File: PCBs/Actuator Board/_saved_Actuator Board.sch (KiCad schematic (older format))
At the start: 14 parts

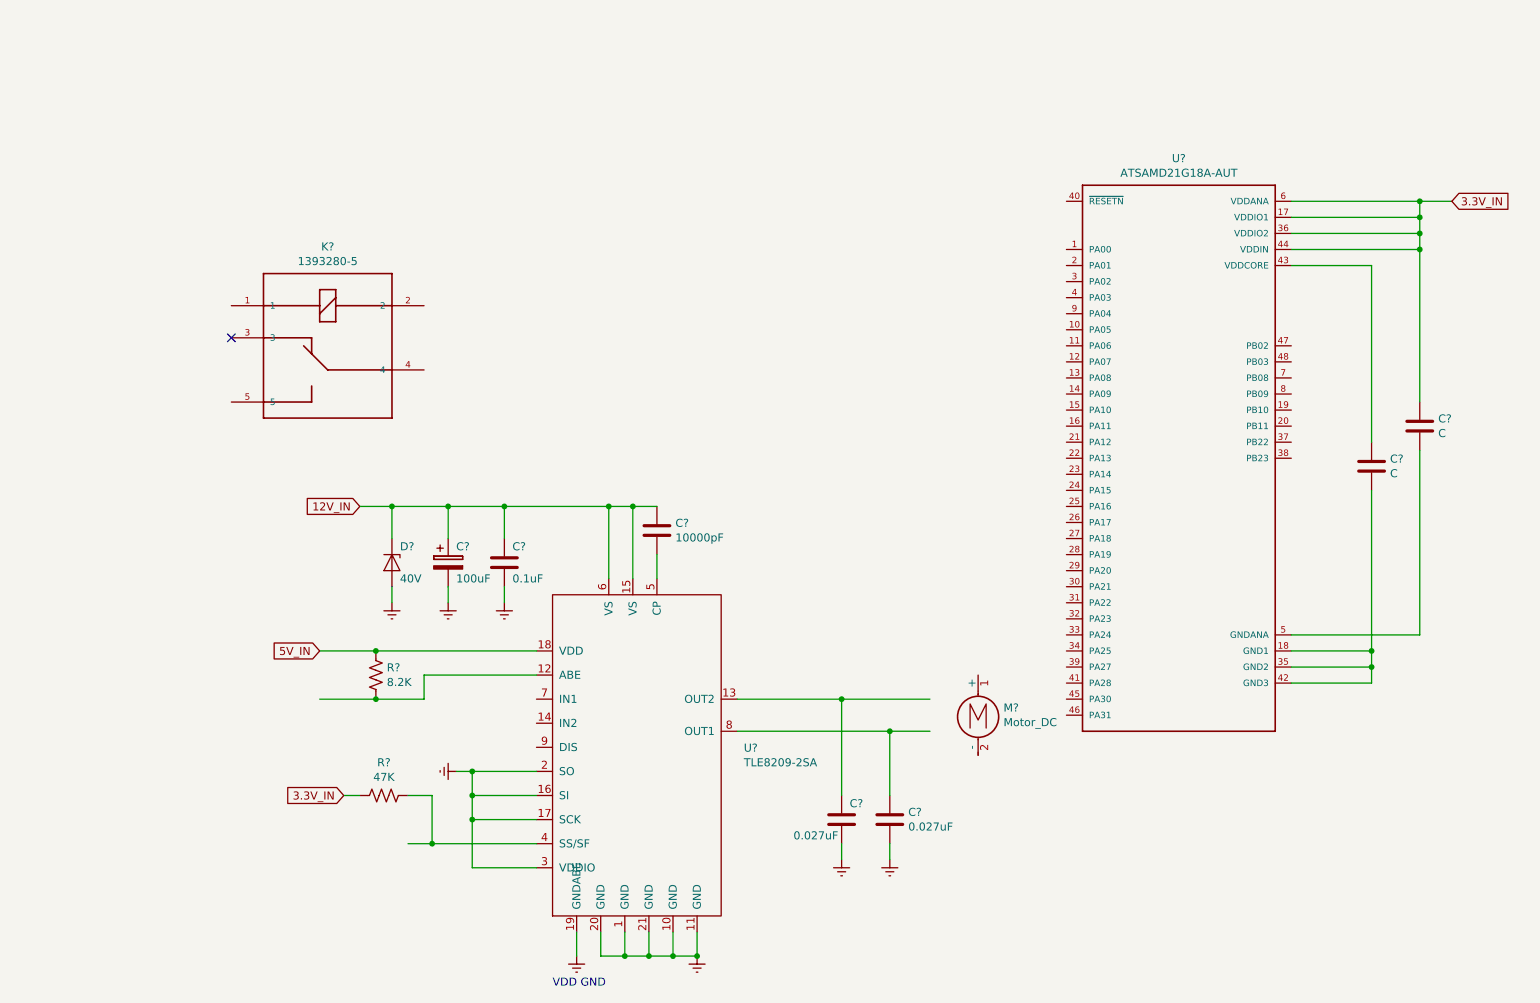
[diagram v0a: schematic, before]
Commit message: Started Relay
finish relay values
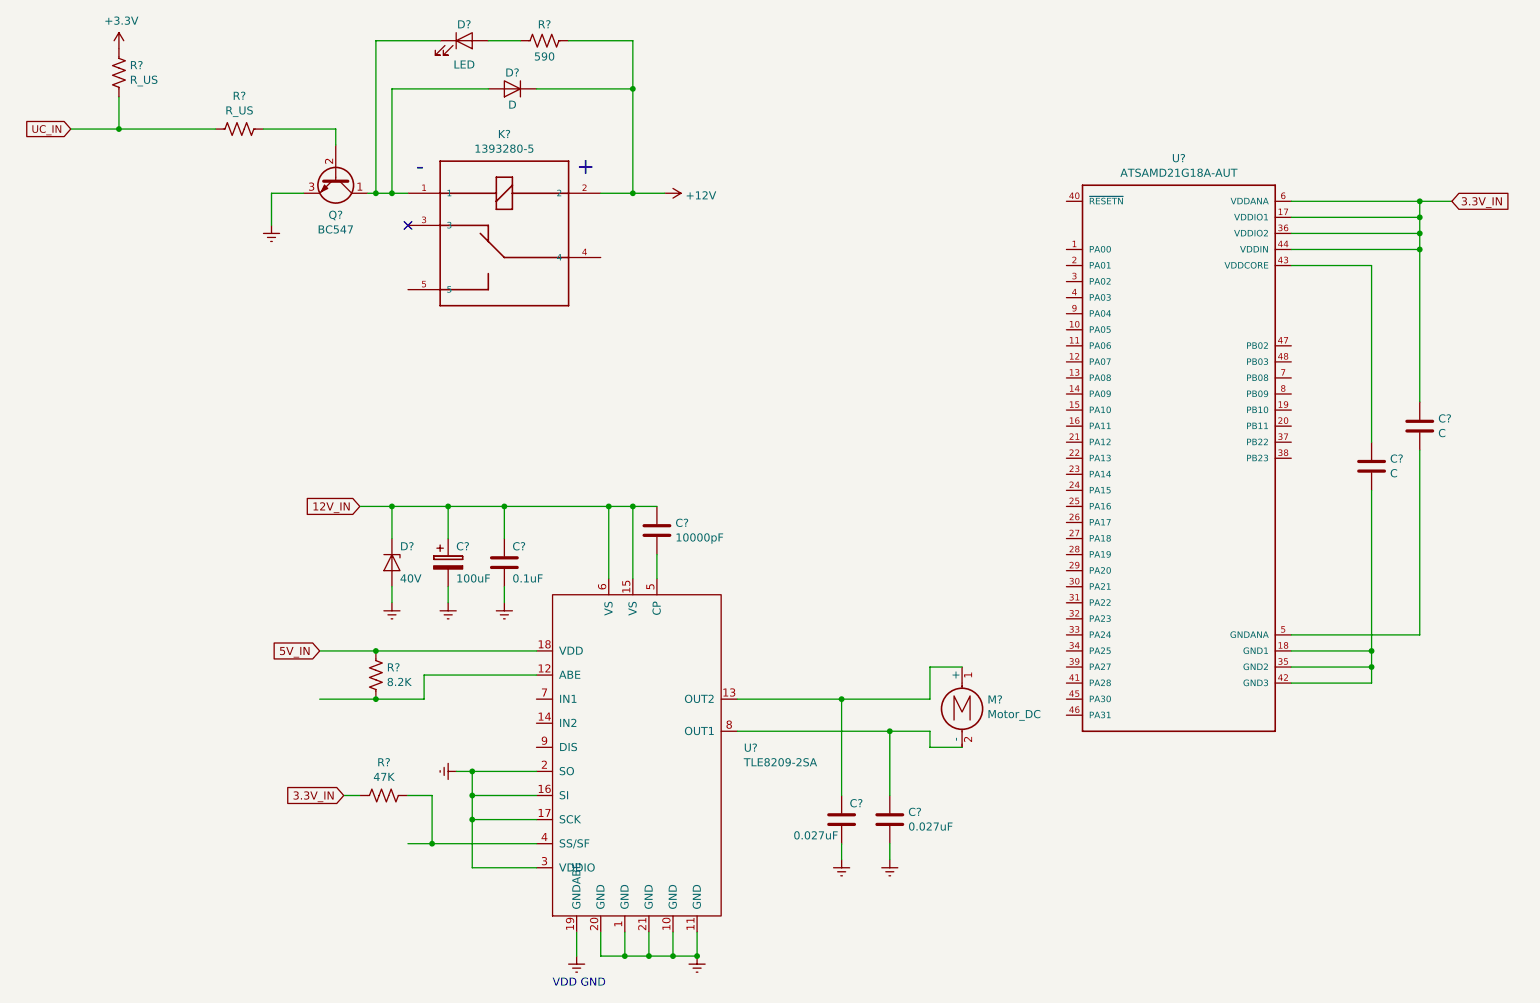
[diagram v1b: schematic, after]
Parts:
- added D?: LED, symbol Device:LED
- added D?: D, symbol Device:D
- added Q?: BC547, Package_TO_SOT_THT:TO-92_Inline, symbol Transistor_BJT:BC547
- added R?: 590, symbol Device:R_US
- added R? (x2): R_US, symbol Device:R_US
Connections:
- net labels added: +12V, +3.3V, UC_IN
- wire segments 71 -> 96
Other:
- note added: "+"
- note added: "-\n"
- moved on the sheet: K?, M?
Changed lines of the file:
@@
 L 1393280-5:1393280-5 K?
 U 1 1 5BD47A2C
-P 3500 2600
-F 0 "K?" H 3500 3267 50  0000 C CNN
-F 1 "1393280-5" H 3500 3176 50  0000 C CNN
-F 2 "RELAY_1393280-5" H 3500 2600 50  0001 L BNN
-F 3 "Electromechanical Relay 12VDC 254Ohm SPST-NO_13.2x12.2x10.1_mm THT Automotive Relay Automotive" H 3500 2600 50  0001 L BNN
-F 4 "None" H 3500 2600 50  0001 L BNN "Field4"
-F 5 "1393280-5" H 3500 2600 50  0001 L BNN "Field5"
-F 6 "https://www.digikey.ca/product-detail/en/te-connectivity-potter-brumfield-relays/1393280-5/PB1977-ND/4581694?utm_source=snapeda&utm_medium=aggregator&utm_campaign=symbol" H 3500 2600 50  0001 L BNN "Field6"
-F 7 "TE Connectivity" H 3500 2600 50  0001 L BNN "Field7"
-F 8 "PB1977-ND" H 3500 2600 50  0001 L BNN "Field8"
-	1    3500 2600
+P 4600 1900
+F 0 "K?" H 4600 2567 50  0000 C CNN
+F 1 "1393280-5" H 4600 2476 50  0000 C CNN
+F 2 "RELAY_1393280-5" H 4600 1900 50  0001 L BNN
+F 3 "Electromechanical Relay 12VDC 254Ohm SPST-NO_13.2x12.2x10.1_mm THT Automotive Relay Automotive" H 4600 1900 50  0001 L BNN
+F 4 "None" H 4600 1900 50  0001 L BNN "Field4"
+F 5 "1393280-5" H 4600 1900 50  0001 L BNN "Field5"
+F 6 "https://www.digikey.ca/product-detail/en/te-connectivity-potter-brumfield-relays/1393280-5/PB1977-ND/4581694?utm_source=snapeda&utm_medium=aggregator&utm_campaign=symbol" H 4600 1900 50  0001 L BNN "Field6"
+F 7 "TE Connectivity" H 4600 1900 50  0001 L BNN "Field7"
+F 8 "PB1977-ND" H 4600 1900 50  0001 L BNN "Field8"
+	1    4600 1900
 	1    0    0    -1
 $EndComp
@@
 	1    0    0    -1
 $EndComp
-NoConn ~ 2900 2500
+NoConn ~ 4000 1800
 Wire Wire Line
 	9500 1650 10300 1650
@@
 L Motor:Motor_DC M?
 U 1 1 5BDF467F
-P 7550 4800
-F 0 "M?" H 7708 4796 50  0000 L CNN
-F 1 "Motor_DC" H 7708 4705 50  0000 L CNN
-F 2 "" H 7550 4710 50  0001 C CNN
-F 3 "~" H 7550 4710 50  0001 C CNN
-	1    7550 4800
+P 7450 4750
+F 0 "M?" H 7608 4746 50  0000 L CNN
+F 1 "Motor_DC" H 7608 4655 50  0000 L CNN
+F 2 "" H 7450 4660 50  0001 C CNN
+F 3 "~" H 7450 4660 50  0001 C CNN
+	1    7450 4750
 	1    0    0    -1
 $EndComp
 Text GLabel 3700 3550 0    50   Input ~ 0
 12V_IN
+Wire Wire Line
+	7250 4750 7250 4550
+Wire Wire Line
+	7250 4550 7450 4550
+Wire Wire Line
+	7250 4950 7250 5050
+Wire Wire Line
+	7250 5050 7450 5050
+$Comp
+L Device:R_US R?
+U 1 1 5BDF7B59
+P 4850 650
+F 0 "R?" V 4750 650 50  0000 C CNN
+F 1 "590" V 4950 650 50  0000 C CNN
+F 2 "" V 4890 640 50  0001 C CNN
+F 3 "~" H 4850 650 50  0001 C CNN
+	1    4850 650
+	0    1    1    0
+$EndComp
+$Comp
+L Device:R_US R?
+U 1 1 5BDF7BA9
+P 2950 1200
+F 0 "R?" V 2745 1200 50  0000 C CNN
+F 1 "R_US" V 2836 1200 50  0000 C CNN
+F 2 "" V 2990 1190 50  0001 C CNN
+F 3 "~" H 2950 1200 50  0001 C CNN
+	1    2950 1200
+	0    1    1    0
+$EndComp
+$Comp
+L Device:R_US R?
+U 1 1 5BDF7BDD
+P 2200 850
+F 0 "R?" H 2268 896 50  0000 L CNN
+F 1 "R_US" H 2268 805 50  0000 L CNN
+F 2 "" V 2240 840 50  0001 C CNN
+F 3 "~" H 2200 850 50  0001 C CNN
+	1    2200 850
+	1    0    0    -1
+$EndComp
+$Comp
+L Device:LED D?
+U 1 1 5BDF7C3A
+P 4350 650
+F 0 "D?" H 4350 750 50  0000 C CNN
+F 1 "LED" H 4350 500 50  0000 C CNN
+F 2 "" H 4350 650 50  0001 C CNN
+F 3 "~" H 4350 650 50  0001 C CNN
+	1    4350 650
+	1    0    0    -1
+$EndComp
+$Comp
+L Device:D D?
+U 1 1 5BDF7C9B
+P 4650 950
+F 0 "D?" H 4650 850 50  0000 C CNN
+F 1 "D" H 4650 1050 50  0000 C CNN
+F 2 "" H 4650 950 50  0001 C CNN
+F 3 "~" H 4650 950 50  0001 C CNN
+	1    4650 950
+	-1   0    0    1
+$EndComp
+Text Notes 5050 1500 0    98   ~ 0
++
+Text Notes 4050 1500 0    98   ~ 0
+-\n
+Wire Wire Line
+	5200 1600 5400 1600
+$Comp
+L Transistor_BJT:BC547 Q?
+U 1 1 5BDFB8ED
+P 3550 1500
+F 0 "Q?" V 3786 1500 50  0000 C CNN
+F 1 "BC547" V 3877 1500 50  0000 C CNN
+F 2 "Package_TO_SOT_THT:TO-92_Inline" H 3750 1425 50  0001 L CIN
+F 3 "http://www.fairchildsemi.com/ds/BC/BC547.pdf" H 3550 1500 50  0001 L CNN
+	1    3550 1500
+	0    1    1    0
+$EndComp
+Wire Wire Line
+	3750 1600 3800 1600
+Wire Wire Line
+	3550 1300 3550 1200
+Wire Wire Line
+	3550 1200 3100 1200
+Wire Wire Line
+	1900 1200 2200 1200
+Wire Wire Line
+	2200 1200 2200 1000
+Connection ~ 2200 1200
+Wire Wire Line
+	2200 1200 2800 1200
+$Comp
+L power:+3.3V #PWR?
+U 1 1 5BE1097E
+P 2200 700
+F 0 "#PWR?" H 2200 550 50  0001 C CNN
+F 1 "+3.3V" H 2215 873 50  0000 C CNN
+F 2 "" H 2200 700 50  0001 C CNN
+F 3 "" H 2200 700 50  0001 C CNN
+	1    2200 700
+	1    0    0    -1
+$EndComp
+Text GLabel 1900 1200 0    47   Input ~ 0
+UC_IN
+Wire Wire Line
+	5400 1600 5400 950
+Wire Wire Line
+	5400 950  4800 950
+Connection ~ 5400 1600
+Wire Wire Line
+	5400 1600 5600 1600
+Wire Wire Line
+	5400 950  5400 650
+Wire Wire Line
+	5400 650  5000 650
+Connection ~ 5400 950
+Wire Wire Line
+	4700 650  4500 650
+Wire Wire Line
+	4200 650  3800 650
+Wire Wire Line
+	3800 650  3800 1600
+Connection ~ 3800 1600
+Wire Wire Line
+	3800 1600 3900 1600
+Wire Wire Line
+	4500 950  3900 950
+Wire Wire Line
+	3900 950  3900 1600
+Connection ~ 3900 1600
+Wire Wire Line
+	3900 1600 4000 1600
+$Comp
+L power:+12V #PWR?
+U 1 1 5BE2D8C2
+P 5600 1600
+F 0 "#PWR?" H 5600 1450 50  0001 C CNN
+F 1 "+12V" V 5615 1728 50  0000 L CNN
+F 2 "" H 5600 1600 50  0001 C CNN
+F 3 "" H 5600 1600 50  0001 C CNN
+	1    5600 1600
+	0    1    1    0
+$EndComp
+Wire Wire Line
+	3350 1600 3150 1600
+Wire Wire Line
+	3150 1600 3150 1800
+$Comp
+L power:Earth #PWR?
+U 1 1 5BE306B3
+P 3150 1800
+F 0 "#PWR?" H 3150 1550 50  0001 C CNN
+F 1 "Earth" H 3150 1650 50  0001 C CNN
+F 2 "" H 3150 1800 50  0001 C CNN
+F 3 "~" H 3150 1800 50  0001 C CNN
+	1    3150 1800
+	1    0    0    -1
+$EndComp
 $EndSCHEMATC
